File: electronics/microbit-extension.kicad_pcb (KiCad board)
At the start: 2 copper layers, 42.5 x 59.7 mm, 31 parts, among them J1 microbit_edge_connector, J2 9V conn, SW1 SW_DIP_x01, SW2 SW_DIP_x01, SW3 SW_DIP_x01, SW4 SW_DIP_x01, T1 2N4401, U1 LD1117S33CTR

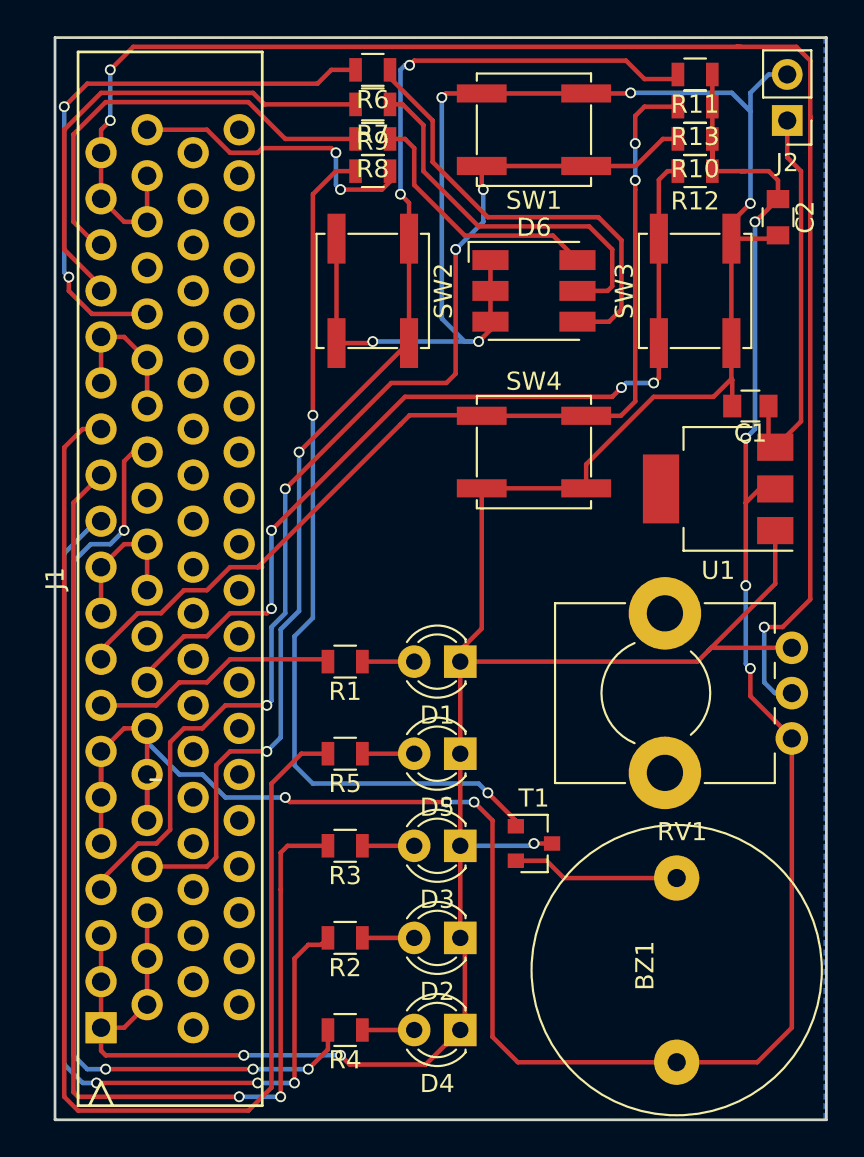
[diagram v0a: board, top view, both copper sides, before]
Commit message: fixed silkscreen
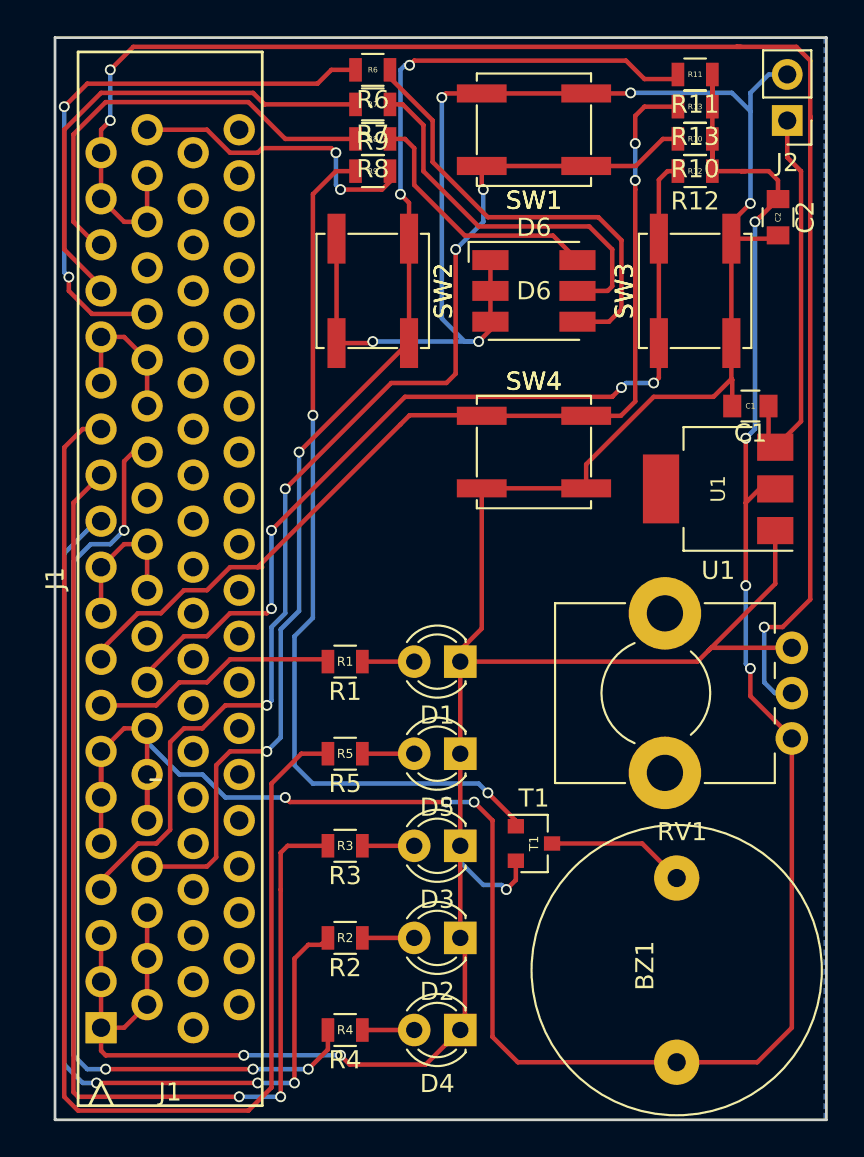
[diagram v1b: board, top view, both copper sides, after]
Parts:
- BZ1: footprint Buzzers_Beepers:BUZZER -> footprints:BUZZER
- C1, C2: footprint Capacitors_SMD:C_0805 -> footprints:C_0805
- D1, D2, D3, D4, D5: footprint LEDs:LED_D3.0mm -> footprints:LED_D3.0mm
- D6: footprint LEDs:LED_RGB_5050-6 -> footprints:LED_RGB_5050-6
- J1: footprint Connectors_4UCON:4UCON_17909_02x401.27mm_Vertical -> footprints:4UCON_17909_02x401.27mm_Vertical
- J2: footprint Pin_Headers:Pin_Header_Straight_1x02_Pitch2.54mm -> footprints:Pin_Header_Straight_1x02_Pitch2.54mm
- R1, R10, R11, R12, R13, R2, R3, R4, R5, R6, R7, R8, R9: footprint Resistors_SMD:R_0805 -> footprints:R_0805
- RV1: footprint Potentiometers:Potentiometer_Alps_RK09K_Horizontal -> footprints:Potentiometer_Alps_RK09K_Horizontal
- SW1, SW2, SW3, SW4: footprint Buttons_Switches_SMD:SW_SPST_EVPBF -> footprints:SW_SPST_EVPBF
- T1: footprint TO_SOT_Packages_SMD:SOT-23 -> footprints:SOT-23
- U1: footprint TO_SOT_Packages_SMD:SOT-223 -> footprints:SOT-223
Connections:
- T1 pad 2: Net-(BZ1-Pad2) -> GND
- T1 pad 3: GND -> Net-(BZ1-Pad2)
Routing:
- net +3V3: track 131.6 -> 133.4 mm
- net Net-(BZ1-Pad2): track 9.27 -> 7.66 mm
- net GND: track 188.4 -> 189.1 mm

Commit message: fixed most things
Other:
- rule pad_to_mask_clearance: 0.2 -> 0
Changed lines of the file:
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@@
     (pad_size 1.524 1.524)
     (pad_drill 0.762)
-    (pad_to_mask_clearance 0.2)
+    (pad_to_mask_clearance 0)
     (aux_axis_origin 0 0)
     (visible_elements FFFCFF7F)
